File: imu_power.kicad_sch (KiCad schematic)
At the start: 12 parts, among them U3 AMS1117-3.3

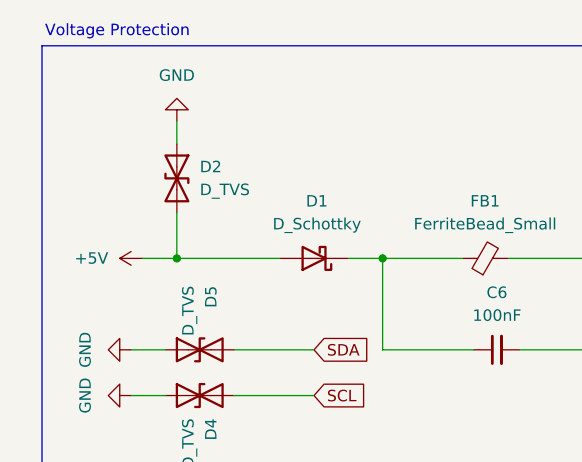
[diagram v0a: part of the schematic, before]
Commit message: Route Traces for ESP32 and related IO
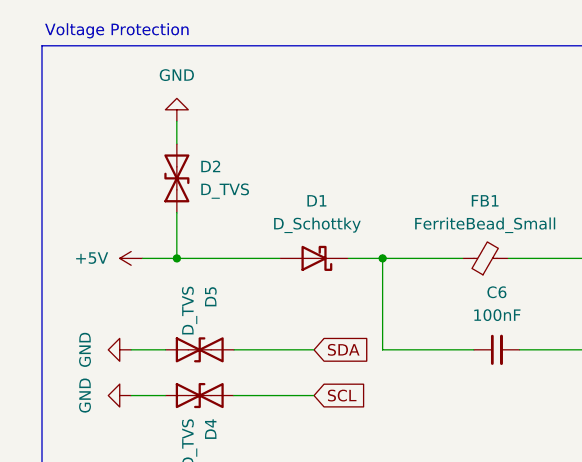
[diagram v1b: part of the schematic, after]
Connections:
- net +5V: now also D2.1 (A1); no longer D2.2 (A2)
- net GND: now also D2.2 (A2); no longer D2.1 (A1)
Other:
- moved on the sheet: D2
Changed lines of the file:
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@@
 	(symbol
 		(lib_id "Device:D_TVS")
-		(at 74.93 76.2 270)
+		(at 74.93 76.2 90)
 		(unit 1)
 		(exclude_from_sim no)
@@
 					(size 1.27 1.27)
 				)
-				(justify left)
+				(justify right)
 			)
 		)
@@
 					(size 1.27 1.27)
 				)
-				(justify left)
+				(justify right)
 			)
 		)

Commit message: Finall Fullboard V1
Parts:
- D2: value D_TVS -> D_TVS0
- D4, D5: value D_TVS -> D_TVS1
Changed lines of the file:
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@@
 			)
 		)
-		(property "Value" "D_TVS"
+		(property "Value" "D_TVS1"
 			(at 76.2001 102.87 90)
 			(effects
@@
 			)
 		)
-		(property "Value" "D_TVS"
+		(property "Value" "D_TVS0"
 			(at 77.47 77.4699 90)
 			(effects
@@
 			)
 		)
-		(property "Value" "D_TVS"
+		(property "Value" "D_TVS1"
 			(at 76.2 88.138 90)
 			(effects
